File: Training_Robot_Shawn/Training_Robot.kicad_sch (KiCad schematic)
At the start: 14 parts, among them J1 Arduino connector, J4 Conn_01x04_Socket, J5 Conn_01x04_Socket, M1 FrontL, M2 FrontR, M3 BackL, M4 BackR, SW1 SW_SPDT_312

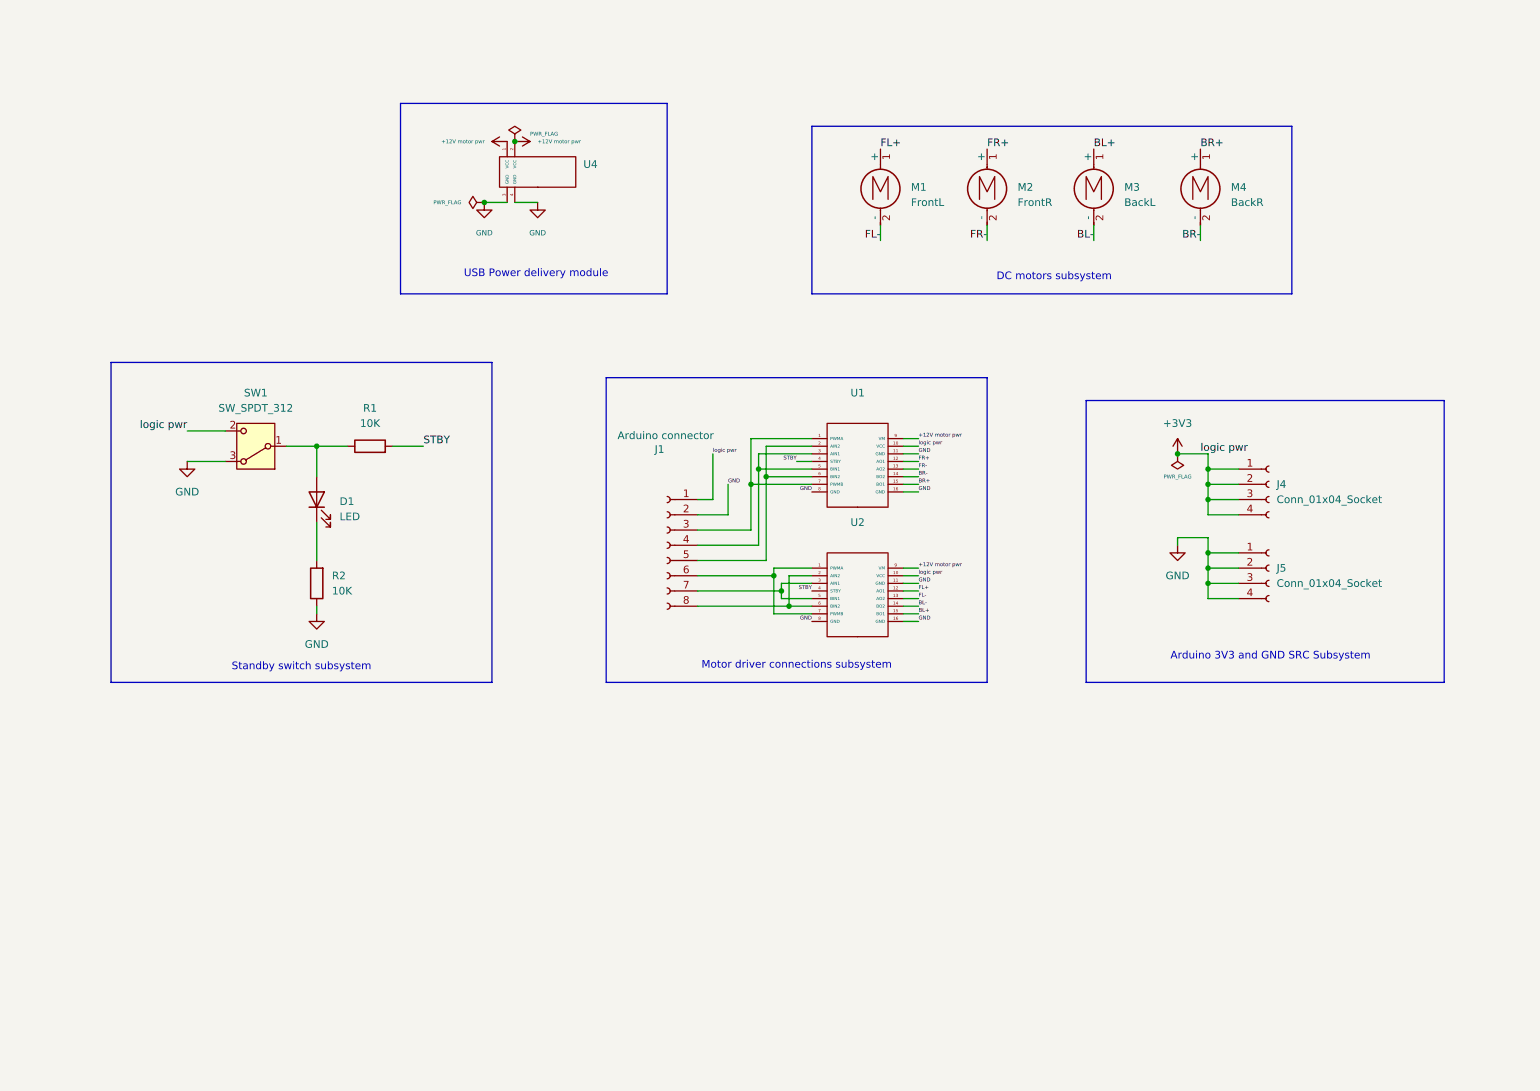
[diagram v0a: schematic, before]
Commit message: Finished schematic and assigned footprints
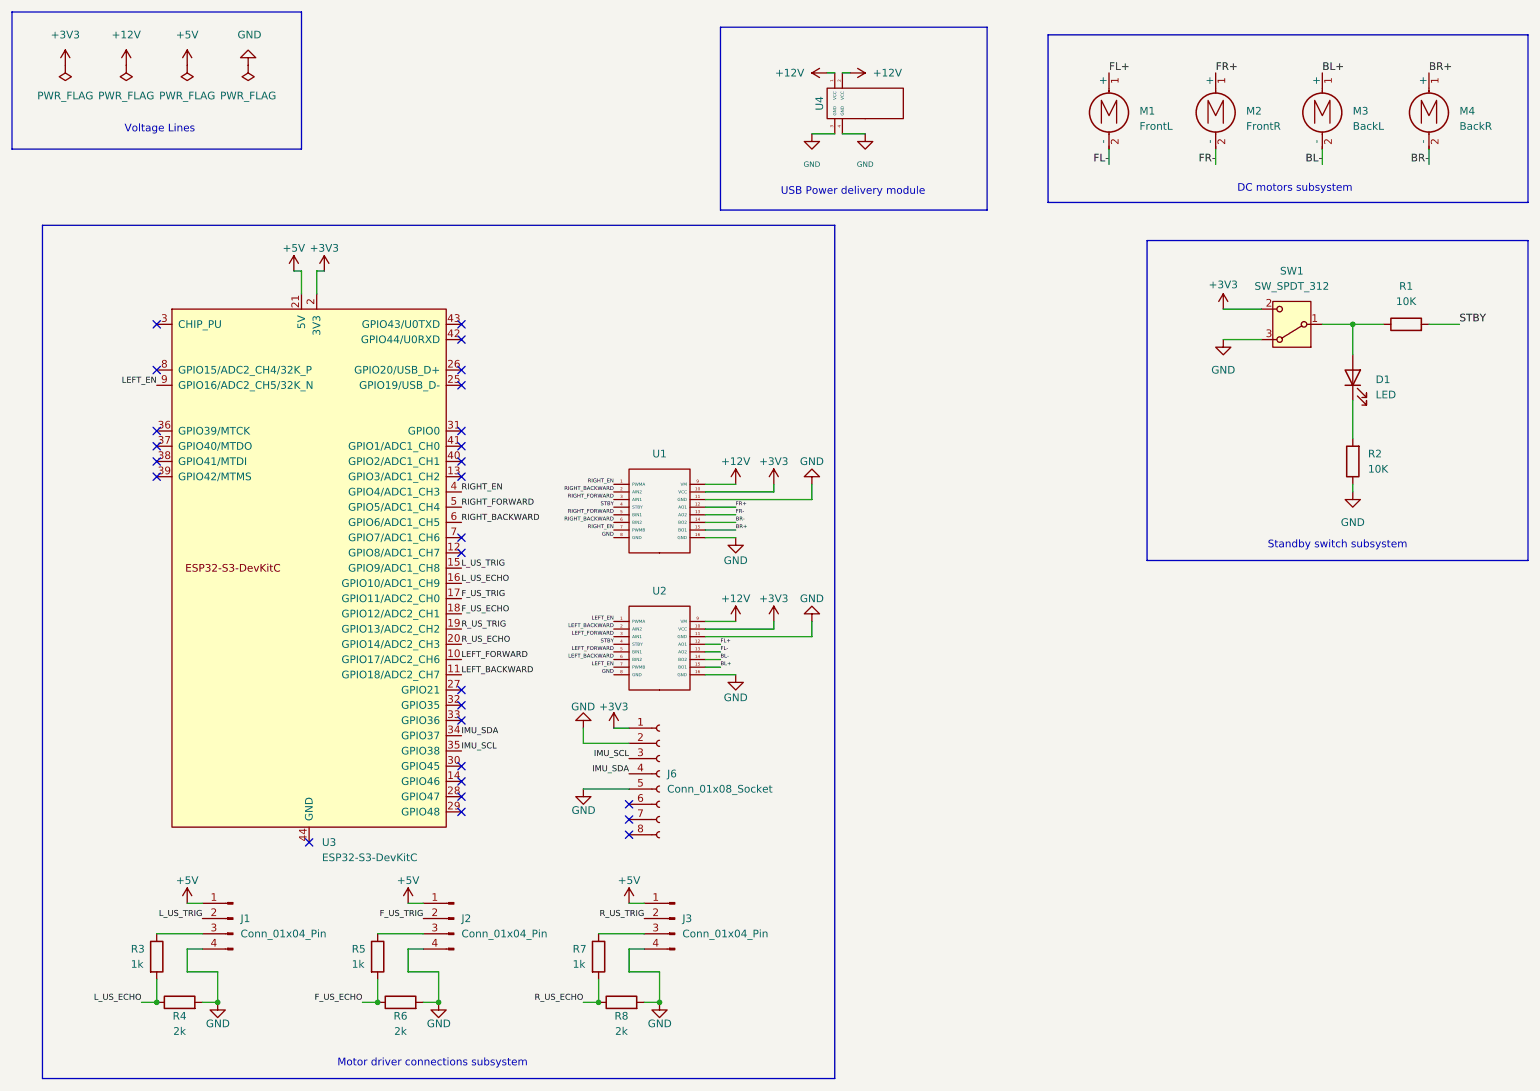
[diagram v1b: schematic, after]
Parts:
- removed J1: Arduino connector, Connector_PinSocket_2.54mm:PinSocket_1x08_P2.54mm_Vertical, symbol Connector:Conn_01x08_Socket
- removed J4, J5: Conn_01x04_Socket, Connector_PinSocket_2.54mm:PinSocket_1x04_P2.54mm_Vertical, symbol Connector:Conn_01x04_Socket
- removed U1, U2: ~, Library:TB_breakout_motor_driver, symbol New_Library:_2
- removed U4: ~, Library:PD Module, symbol New_Library:_3
- added J1, J2, J3: Conn_01x04_Pin, Connector_JST:JST_XH_B4B-XH-A_1x04_P2.50mm_Vertical, symbol Connector:Conn_01x04_Pin
- added J6: Conn_01x08_Socket, Connector_PinSocket_2.54mm:PinSocket_1x08_P2.54mm_Vertical, symbol Connector:Conn_01x08_Socket
- added R3, R5, R7: 1k, Resistor_THT:R_Axial_DIN0204_L3.6mm_D1.6mm_P5.08mm_Horizontal, symbol Device:R
- added R4, R6, R8: 2k, Resistor_THT:R_Axial_DIN0204_L3.6mm_D1.6mm_P5.08mm_Horizontal, symbol Device:R
- added U1, U2: (no value), MARS Custom Footprints:TB6612FNG Breakout, symbol MARS Custom Symbols:Breakout_tb6612FNG
- added U3: ESP32-S3-DevKitC, PCM_Espressif:ESP32-S3-DevKitC, symbol PCM_Espressif:ESP32-S3-DevKitC
- added U4: (no value), MARS Custom Footprints:USB PD Module, symbol MARS Custom Symbols:PD_Module
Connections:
- net +3V3: now also J6.1 (Pin_1), U1.10 (VCC), U2.10 (VCC), U3.1 (3V3), U3.2 (3V3)
- net BL+: now also U2.15 (BO1)
- net BL-: now also U2.14 (BO2)
- net BR+: now also U1.15 (BO1)
- net BR-: now also U1.14 (BO2)
- net FL+: now also U2.12 (AO1)
- net FL-: now also U2.13 (AO2)
- net FR+: now also U1.12 (AO1)
- net FR-: now also U1.13 (AO2)
- net GND: now also J1.4 (Pin_4), J2.4 (Pin_4), J3.4 (Pin_4), J6.2 (Pin_2), J6.5 (Pin_5), R4.2, R6.2, R8.2, U1.11 (GND), U1.16 (GND), U1.8 (GND), U2.11 (GND), U2.16 (GND), U2.8 (GND), U4.3 (GND), U4.4 (GND)
- net STBY: now also U1.4 (STBY), U2.4 (STBY)
- new net: J2.3 (Pin_3), R5.1
- new net: J3.3 (Pin_3), R7.1
- new net: U3.22 (GND), U3.23 (GND), U3.24 (GND), U3.44 (GND)
- new net: J1.3 (Pin_3), R3.1
- new net +12V: U1.9 (VM), U2.9 (VM), U4.1 (VCC), U4.2 (VCC)
- new net +5V: J1.1 (Pin_1), J2.1 (Pin_1), J3.1 (Pin_1), U3.21 (5V)
- new net F_US_ECHO: R5.2, R6.1, U3.18 (GPIO12/ADC2_CH1)
- new net F_US_TRIG: J2.2 (Pin_2), U3.17 (GPIO11/ADC2_CH0)
- new net IMU_SCL: J6.3 (Pin_3), U3.35 (GPIO38)
- new net IMU_SDA: J6.4 (Pin_4), U3.34 (GPIO37)
- new net LEFT_BACKWARD: U2.2 (AIN2), U2.6 (BIN2), U3.11 (GPIO18/ADC2_CH7)
- new net LEFT_EN: U2.1 (PWMA), U2.7 (PWMB), U3.9 (GPIO16/ADC2_CH5/32K_N)
- new net LEFT_FORWARD: U2.3 (AIN1), U2.5 (BIN1), U3.10 (GPIO17/ADC2_CH6)
- new net L_US_ECHO: R3.2, R4.1, U3.16 (GPIO10/ADC1_CH9)
- new net L_US_TRIG: J1.2 (Pin_2), U3.15 (GPIO9/ADC1_CH8)
- new net RIGHT_BACKWARD: U1.2 (AIN2), U1.6 (BIN2), U3.6 (GPIO6/ADC1_CH5)
- new net RIGHT_EN: U1.1 (PWMA), U1.7 (PWMB), U3.4 (GPIO4/ADC1_CH3)
- new net RIGHT_FORWARD: U1.3 (AIN1), U1.5 (BIN1), U3.5 (GPIO5/ADC1_CH4)
- new net R_US_ECHO: R7.2, R8.1, U3.20 (GPIO14/ADC2_CH3)
- new net R_US_TRIG: J3.2 (Pin_2), U3.19 (GPIO13/ADC2_CH2)
- no-connect marks 0 -> 27
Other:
- note added: "Voltage Lines"
- note removed: "Arduino 3V3 and GND SRC Subsystem"
- moved on the sheet: D1, M1, M2, M3, M4, R1, R2, SW1

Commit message: layout edits v2
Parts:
- added H1, H2, H3, H4: MountingHole, MountingHole:MountingHole_4.5mm, symbol Mechanical:MountingHole

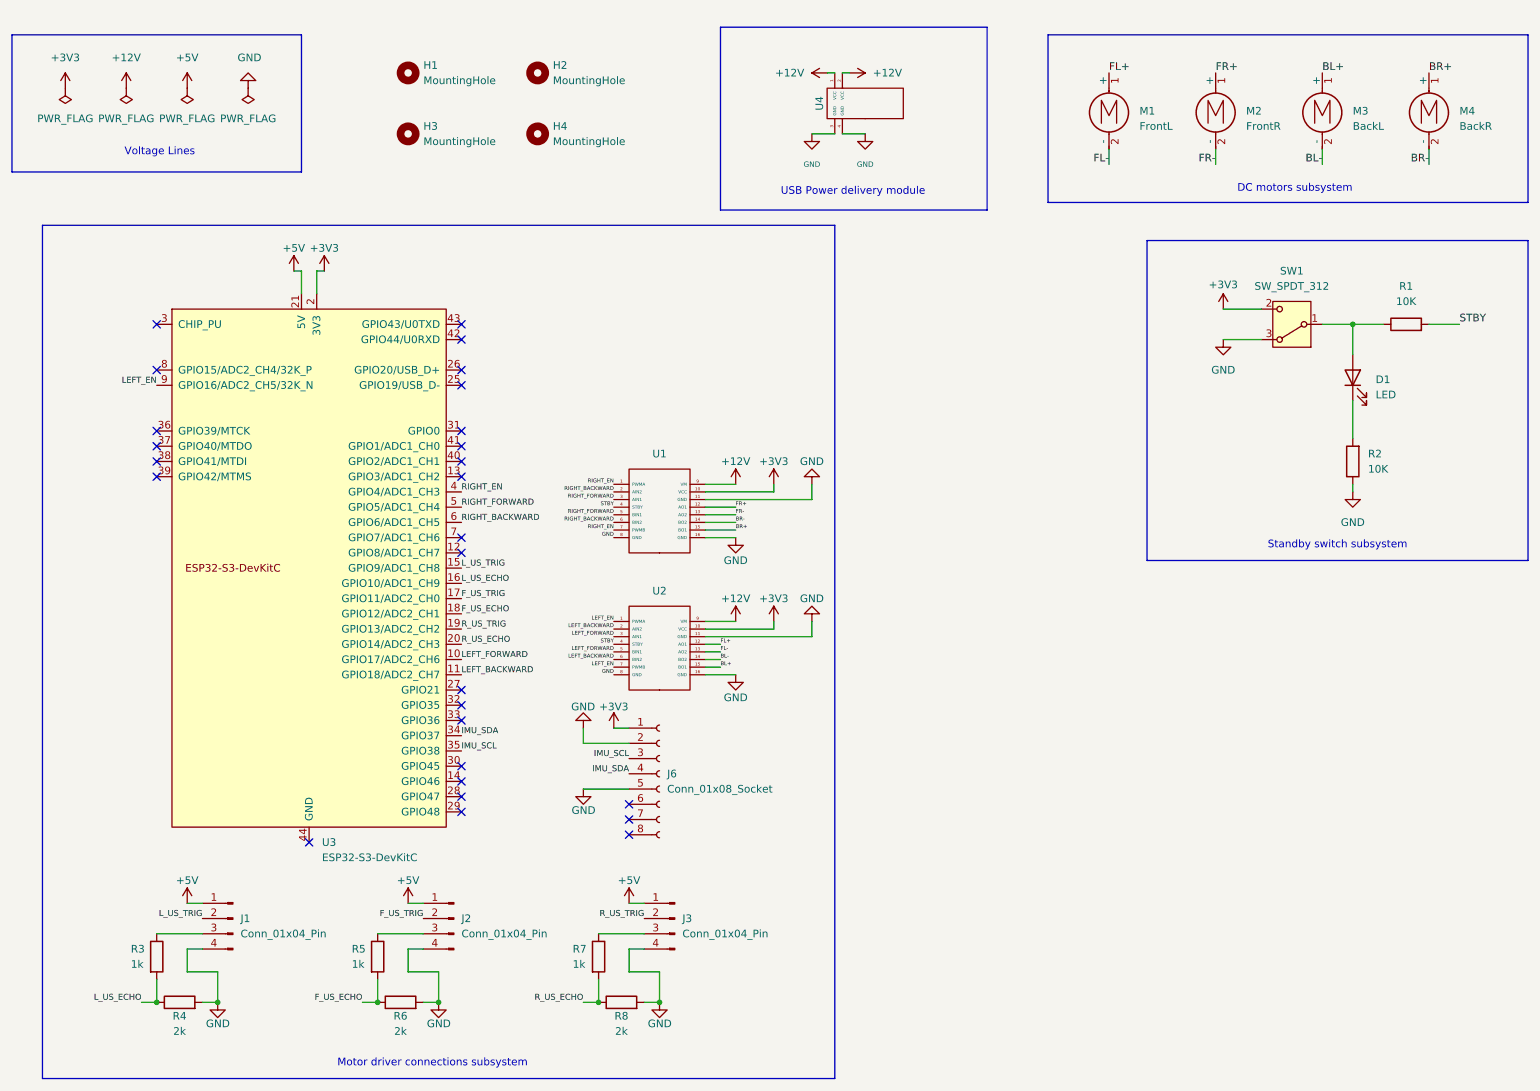
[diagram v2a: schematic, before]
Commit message: schematic changes made
-removed r1
-reduced r2 to 180 ohms
-added fuses for motor drivers
-removed usb pd module and added symbols for xt60 (battery), buck converter, and block terminal (5v)
-only missing fuse footprints
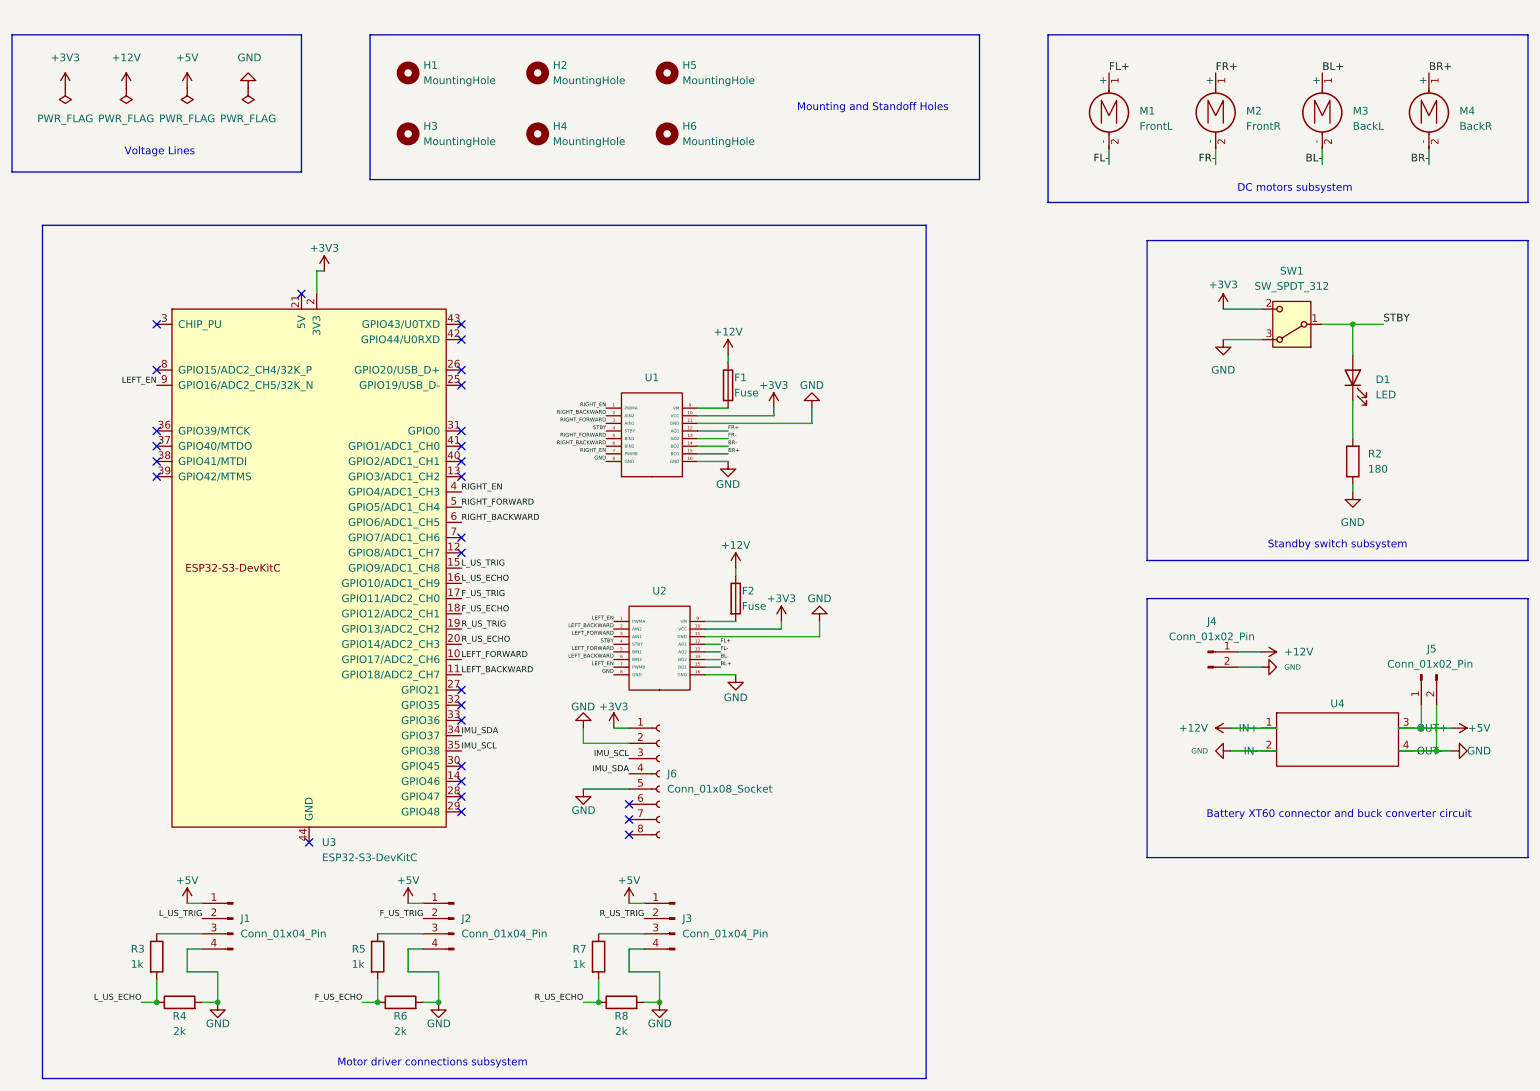
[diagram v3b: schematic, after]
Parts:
- removed R1: 10K, Resistor_THT:R_Axial_DIN0204_L3.6mm_D1.6mm_P5.08mm_Horizontal, symbol Device:R
- removed U4: (no value), MARS Custom Footprints:USB PD Module, symbol MARS Custom Symbols:PD_Module
- added F1, F2: Fuse, symbol Device:Fuse
- added H5, H6: MountingHole, MountingHole:MountingHole_4.5mm, symbol Mechanical:MountingHole
- added J4: Conn_01x02_Pin, MARS Custom Footprints:Amass XT60PW, symbol Connector:Conn_01x02_Pin
- added J5: Conn_01x02_Pin, TerminalBlock_Phoenix:TerminalBlock_Phoenix_MKDS-1,5-2_1x02_P5.00mm_Horizontal, symbol Connector:Conn_01x02_Pin
- added U4: (no value), MARS Custom Footprints:MP1495, symbol MARS Custom Symbols:Generic_Converter
- R2: value 10K -> 180; footprint Resistor_THT:R_Axial_DIN0204_L3.6mm_D1.6mm_P5.08mm_Horizontal -> Resistor_THT:R_Axial_DIN0204_L3.6mm_D1.6mm_P7.62mm_Horizontal
- R3, R4, R5, R6, R7, R8: footprint Resistor_THT:R_Axial_DIN0204_L3.6mm_D1.6mm_P5.08mm_Horizontal -> Resistor_THT:R_Axial_DIN0204_L3.6mm_D1.6mm_P7.62mm_Horizontal
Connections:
- net +12V: now also F1.1, F2.1, J4.1 (Pin_1), U4.1 (IN+); no longer U1.9 (VM), U2.9 (VM)
- net +5V: now also J5.1 (Pin_1), U4.3 (OUT+); no longer U3.21 (5V)
- net GND: now also J4.2 (Pin_2), J5.2 (Pin_2), U4.2 (IN-), U4.4 (OUT-)
- net STBY: now also D1.2 (A), SW1.1 (B)
- new net: F2.2, U2.9 (VM)
- new net: F1.2, U1.9 (VM)
- no-connect marks 27 -> 28
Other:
- note added: "Battery XT60 connector and buck converter circuit"
- note added: "Mounting and Standoff Holes"
- note removed: "USB Power delivery module"
- moved on the sheet: U1

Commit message: finished schematic editing
-added fuse footprint to fuses
-deleted unnecessary mounting previously used for usb pd standoff

additional changes in last commit i forgot (oops)
-changed footprint for resistors to be larger
-removed connection from esp32 5v pin
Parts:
- removed H6: MountingHole, MountingHole:MountingHole_4.5mm, symbol Mechanical:MountingHole
- F1, F2: footprint (none) -> MARS Custom Footprints:01530008Z Fuse Holder
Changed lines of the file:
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@@
 			)
 		)
-		(property "Footprint" ""
+		(property "Footprint" "MARS Custom Footprints:01530008Z Fuse Holder"
 			(at 141.732 113.03 90)
 			(hide yes)
@@
 	)
 	(symbol
-		(lib_id "Mechanical:MountingHole")
-		(at 132.08 35.56 0)
-		(unit 1)
-		(body_style 1)
-		(exclude_from_sim no)
-		(in_bom no)
-		(on_board yes)
-		(in_pos_files yes)
-		(dnp no)
-		(fields_autoplaced yes)
-		(property "Reference" "H6"
-			(at 134.62 34.2899 0)
-			(show_name no)
-			(do_not_autoplace no)
-			(effects
-				(font
-					(size 1.27 1.27)
-				)
-				(justify left)
-			)
-		)
-		(property "Value" "MountingHole"
-			(at 134.62 36.8299 0)
-			(show_name no)
-			(do_not_autoplace no)
-			(effects
-				(font
-					(size 1.27 1.27)
-				)
-				(justify left)
-			)
-		)
-		(property "Footprint" "MountingHole:MountingHole_4.5mm"
-			(at 132.08 35.56 0)
-			(hide yes)
-			(show_name no)
-			(do_not_autoplace no)
-			(effects
-				(font
-					(size 1.27 1.27)
-				)
-			)
-		)
-		(property "Datasheet" "~"
-			(at 132.08 35.56 0)
-			(hide yes)
-			(show_name no)
-			(do_not_autoplace no)
-			(effects
-				(font
-					(size 1.27 1.27)
-				)
-			)
-		)
-		(property "Description" "Mounting Hole without connection"
-			(at 132.08 35.56 0)
-			(hide yes)
-			(show_name no)
-			(do_not_autoplace no)
-			(effects
-				(font
-					(size 1.27 1.27)
-				)
-			)
-		)
-		(instances
-			(project "Training_Robot"
-				(path "/53f0e706-6ac7-4906-8109-2d499eeefa1f"
-					(reference "H6")
-					(unit 1)
-				)
-			)
-		)
-	)
-	(symbol
 		(lib_id "MARS Custom Symbols:Breakout_tb6612FNG")
 		(at 129.54 85.09 0)
@@
 			)
 		)
-		(property "Footprint" ""
+		(property "Footprint" "MARS Custom Footprints:01530008Z Fuse Holder"
 			(at 140.462 77.47 90)
 			(hide yes)

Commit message: add uncompleted layout
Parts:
- U3: footprint PCM_Espressif:ESP32-S3-DevKitC -> Espressif:ESP32-S3-DevKitC
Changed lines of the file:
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@@
 			)
 		)
-		(property "Footprint" "PCM_Espressif:ESP32-S3-DevKitC"
+		(property "Footprint" "Espressif:ESP32-S3-DevKitC"
 			(at 72.39 165.1 0)
 			(hide yes)

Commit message: add all components except for buck converter
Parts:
- F1, F2: footprint MARS Custom Footprints:01530008Z Fuse Holder -> 01530008Z:01530008
- J4: footprint MARS Custom Footprints:Amass XT60PW -> TerminalBlock_Phoenix:TerminalBlock_Phoenix_MKDS-1,5-2_1x02_P5.00mm_Horizontal
- U1, U2: footprint MARS Custom Footprints:TB6612FNG Breakout -> ROB-14450:MODULE_ROB-14450
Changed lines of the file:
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@@
 			)
 		)
-		(property "Footprint" "MARS Custom Footprints:01530008Z Fuse Holder"
+		(property "Footprint" "01530008Z:01530008"
 			(at 141.732 113.03 90)
 			(hide yes)
@@
 			)
 		)
-		(property "Footprint" "MARS Custom Footprints:TB6612FNG Breakout"
+		(property "Footprint" "ROB-14450:MODULE_ROB-14450"
 			(at 129.54 85.09 0)
 			(hide yes)
@@
 			)
 		)
-		(property "Footprint" "MARS Custom Footprints:01530008Z Fuse Holder"
+		(property "Footprint" "01530008Z:01530008"
 			(at 140.462 77.47 90)
 			(hide yes)
@@
 			)
 		)
-		(property "Footprint" "MARS Custom Footprints:TB6612FNG Breakout"
+		(property "Footprint" "ROB-14450:MODULE_ROB-14450"
 			(at 130.81 120.65 0)
 			(hide yes)
@@
 			)
 		)
-		(property "Footprint" "MARS Custom Footprints:Amass XT60PW"
+		(property "Footprint" "TerminalBlock_Phoenix:TerminalBlock_Phoenix_MKDS-1,5-2_1x02_P5.00mm_Horizontal"
 			(at 222.25 121.92 0)
 			(hide yes)
